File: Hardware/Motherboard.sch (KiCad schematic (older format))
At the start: 14 parts, among them J2 Conn_01x05_Male, J6 USB, U1 PIC18F46K22-xPT

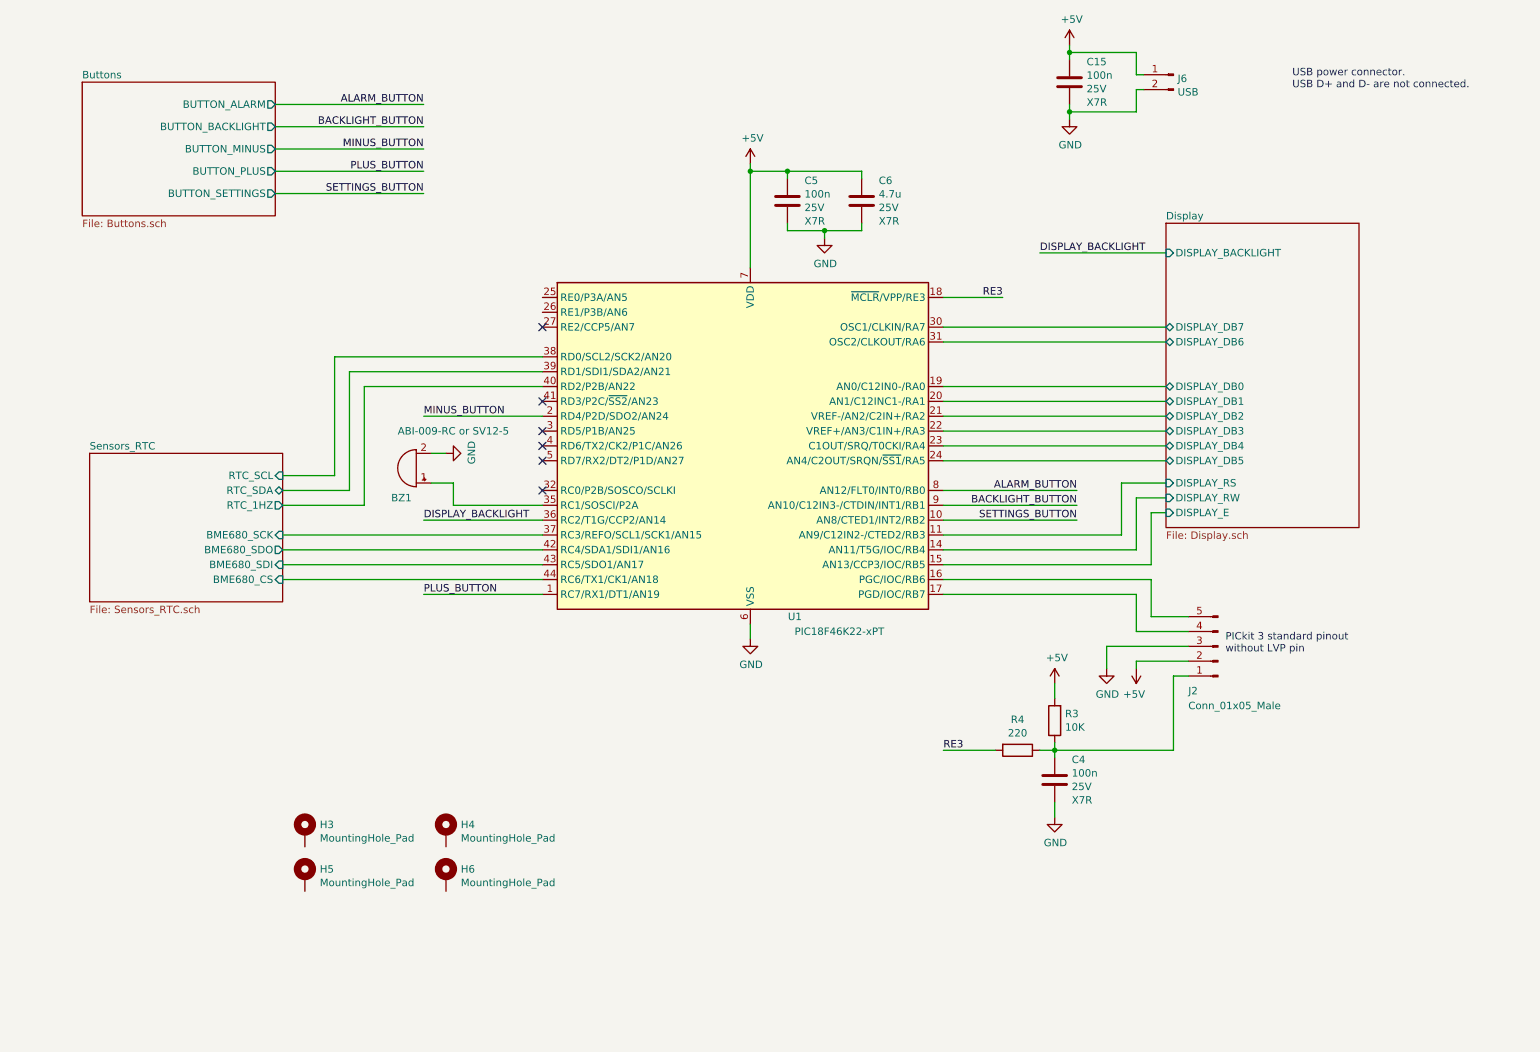
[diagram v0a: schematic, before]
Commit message: [Hardware] Swapped programming connector to have it in the right order.
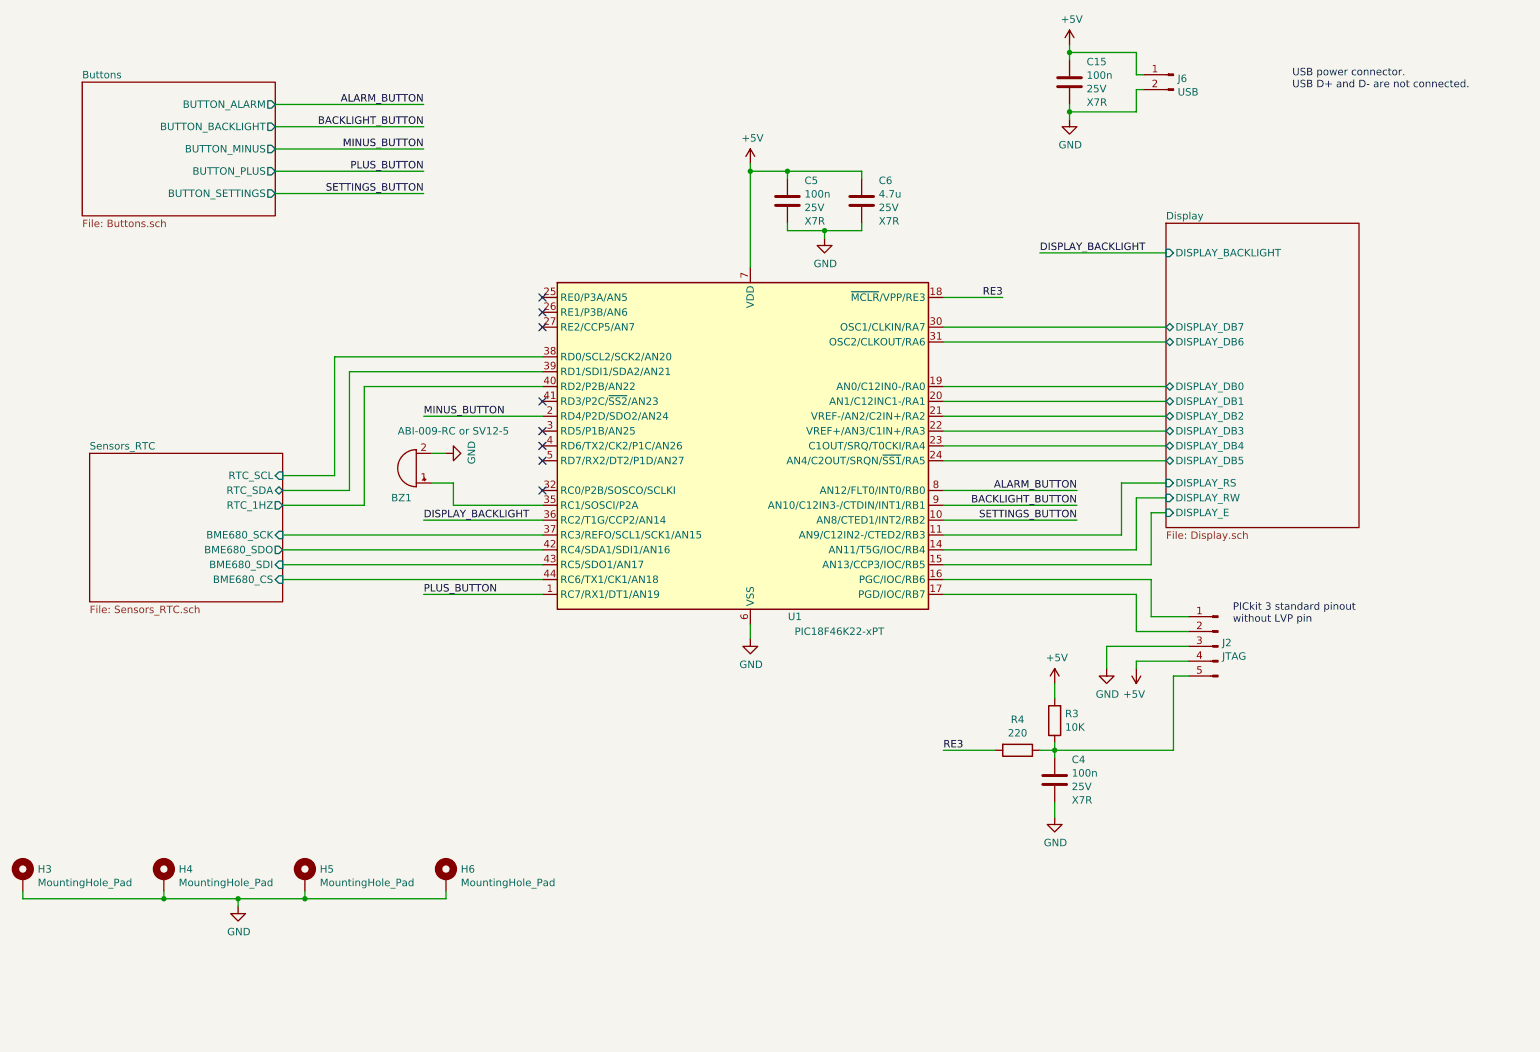
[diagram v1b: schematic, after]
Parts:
- J2: value Conn_01x05_Male -> JTAG
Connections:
- net +5V: now also J2.4 (Pin_4); no longer J2.2 (Pin_2)
- net GND: now also H3.1, H4.1, H5.1, H6.1
- net at C4.1, R3.1, R4.1: now also J2.5 (Pin_5); no longer J2.1 (Pin_1)
- net at U1.17 (PGD/IOC/RB7): now also J2.2 (Pin_2); no longer J2.4 (Pin_4)
- net at U1.16 (PGC/IOC/RB6): now also J2.1 (Pin_1); no longer J2.5 (Pin_5)
- no-connect marks 6 -> 8
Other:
- moved on the sheet: H3, H4
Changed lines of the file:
@@
 U 1 1 5E7B1C5C
 P 9100 4850
-F 0 "J2" H 9300 5150 50  0000 R CNN
-F 1 "Conn_01x05_Male" H 9300 5250 50  0000 R CNN
+F 0 "J2" H 9072 4874 50  0000 R CNN
+F 1 "JTAG" H 9072 4783 50  0000 R CNN
 F 2 "Connector_PinHeader_2.54mm:PinHeader_1x05_P2.54mm_Horizontal" H 9100 4850 50  0001 C CNN
 F 3 "~" H 9100 4850 50  0001 C CNN
 	1    9100 4850
-	-1   0    0    1
-$EndComp
-Text Notes 9150 4900 0    50   ~ 0
+	-1   0    0    -1
+$EndComp
+Text Notes 9200 4700 0    50   ~ 0
 PICkit 3 standard pinout\nwithout LVP pin
 $Comp
@@
 L Mechanical:MountingHole_Pad H3
 U 1 1 5E7D4D02
-P 2950 6100
-F 0 "H3" H 3050 6149 50  0000 L CNN
-F 1 "MountingHole_Pad" H 3050 6058 50  0000 L CNN
-F 2 "MountingHole:MountingHole_4.5mm_Pad" H 2950 6100 50  0001 C CNN
-F 3 "~" H 2950 6100 50  0001 C CNN
-	1    2950 6100
+P 1050 6400
+F 0 "H3" H 1150 6449 50  0000 L CNN
+F 1 "MountingHole_Pad" H 1150 6358 50  0000 L CNN
+F 2 "MountingHole:MountingHole_4.5mm_Pad" H 1050 6400 50  0001 C CNN
+F 3 "~" H 1050 6400 50  0001 C CNN
+	1    1050 6400
 	1    0    0    -1
 $EndComp
@@
 L Mechanical:MountingHole_Pad H4
 U 1 1 5E7D5632
-P 3900 6100
-F 0 "H4" H 4000 6149 50  0000 L CNN
-F 1 "MountingHole_Pad" H 4000 6058 50  0000 L CNN
-F 2 "MountingHole:MountingHole_4.5mm_Pad" H 3900 6100 50  0001 C CNN
-F 3 "~" H 3900 6100 50  0001 C CNN
-	1    3900 6100
+P 2000 6400
+F 0 "H4" H 2100 6449 50  0000 L CNN
+F 1 "MountingHole_Pad" H 2100 6358 50  0000 L CNN
+F 2 "MountingHole:MountingHole_4.5mm_Pad" H 2000 6400 50  0001 C CNN
+F 3 "~" H 2000 6400 50  0001 C CNN
+	1    2000 6400
 	1    0    0    -1
 $EndComp
@@
 Text Label 3750 1800 2    50   ~ 0
 SETTINGS_BUTTON
+NoConn ~ 4550 2500
+NoConn ~ 4550 2600
+$Comp
+L power:GND #PWR0123
+U 1 1 5E7E3802
+P 2500 6600
+F 0 "#PWR0123" H 2500 6350 50  0001 C CNN
+F 1 "GND" H 2505 6427 50  0000 C CNN
+F 2 "" H 2500 6600 50  0001 C CNN
+F 3 "" H 2500 6600 50  0001 C CNN
+	1    2500 6600
+	1    0    0    -1
+$EndComp
+Wire Wire Line
+	1050 6500 1050 6550
+Wire Wire Line
+	1050 6550 2000 6550
+Wire Wire Line
+	2000 6550 2000 6500
+Wire Wire Line
+	2000 6550 2500 6550
+Wire Wire Line
+	2950 6550 2950 6500
+Connection ~ 2000 6550
+Wire Wire Line
+	3900 6550 3900 6500
+Wire Wire Line
+	2500 6600 2500 6550
+Connection ~ 2500 6550
+Wire Wire Line
+	2500 6550 2950 6550
+Wire Wire Line
+	2950 6550 3900 6550
+Connection ~ 2950 6550
 $EndSCHEMATC

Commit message: [Hardware] Added USB connector supply part to both schematic and PCB.
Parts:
- added J7: MUSBD111M0_Supply, Empty_Footprint:Empty_Footprint, symbol USB_Connector_MUSBD111M0:MUSBD111M0_Supply
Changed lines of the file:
@@
 	2950 6550 3900 6550
 Connection ~ 2950 6550
+$Comp
+L USB_Connector_MUSBD111M0:MUSBD111M0_Supply J7
+U 1 1 5E7EC2F9
+P 5050 7150
+F 0 "J7" H 5428 7196 50  0000 L CNN
+F 1 "MUSBD111M0_Supply" H 5428 7105 50  0000 L CNN
+F 2 "Empty_Footprint:Empty_Footprint" H 5050 7150 50  0001 C CNN
+F 3 "" H 5050 7150 50  0001 C CNN
+	1    5050 7150
+	1    0    0    -1
+$EndComp
 $EndSCHEMATC

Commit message: [Hardware] Replaced each supply part by a generic one to avoid creating a new symbol for every supply part.
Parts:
- removed J7: MUSBD111M0_Supply, Empty_Footprint:Empty_Footprint, symbol USB_Connector_MUSBD111M0:MUSBD111M0_Supply
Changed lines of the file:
@@
 $Descr A4 11693 8268
 encoding utf-8
-Sheet 1 4
+Sheet 1 5
 Title "Clock 2 motherboard"
 Date ""
@@
 	2950 6550 3900 6550
 Connection ~ 2950 6550
-$Comp
-L USB_Connector_MUSBD111M0:MUSBD111M0_Supply J7
-U 1 1 5E7EC2F9
-P 5050 7150
-F 0 "J7" H 5428 7196 50  0000 L CNN
-F 1 "MUSBD111M0_Supply" H 5428 7105 50  0000 L CNN
-F 2 "Empty_Footprint:Empty_Footprint" H 5050 7150 50  0001 C CNN
-F 3 "" H 5050 7150 50  0001 C CNN
-	1    5050 7150
-	1    0    0    -1
-$EndComp
+$Sheet
+S 5050 6900 1000 500
+U 5EA3776E
+F0 "Supplies" 50
+F1 "Supplies.sch" 50
+$EndSheet
 $EndSCHEMATC

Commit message: [Hardware] Swapped 'plus' and 'minus' buttons in both schematic and PCB to match final buttons position.
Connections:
- net MINUS_BUTTON: now also U1.1 (RC7/RX1/DT1/AN19); no longer U1.2 (RD4/P2D/SDO2/AN24)
- net PLUS_BUTTON: now also U1.2 (RD4/P2D/SDO2/AN24); no longer U1.1 (RC7/RX1/DT1/AN19)
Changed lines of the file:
@@
 	4550 4500 3750 4500
 Text Label 3750 4500 0    50   ~ 0
-PLUS_BUTTON
+MINUS_BUTTON
 Wire Wire Line
 	2750 1650 3750 1650
@@
 	4550 3300 3750 3300
 Text Label 3750 3300 0    50   ~ 0
-MINUS_BUTTON
+PLUS_BUTTON
 Wire Wire Line
 	2750 1500 3750 1500
